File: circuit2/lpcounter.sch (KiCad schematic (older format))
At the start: 28 parts, among them IC1 ATTINY85V-P, M1 SYN115, P1 CONN_01X08, P10 BAT-, P2 CONN_02X01, P3 Hole_3.5mm, P4 Hole_3.5mm, P5 Hole_3.5mm, P6 Hole_3.5mm, P7 BAT+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

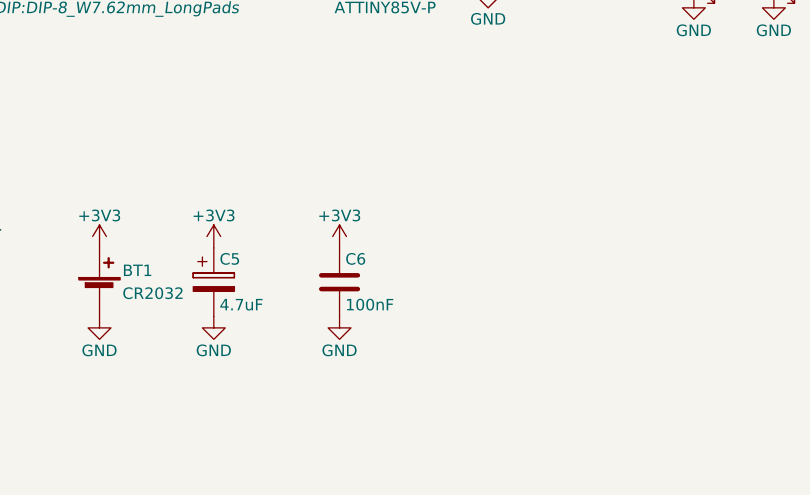
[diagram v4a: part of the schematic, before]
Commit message: small PCB optimizations, moving screw connector away from CR2032 battery add top zone layer and capacitor on top
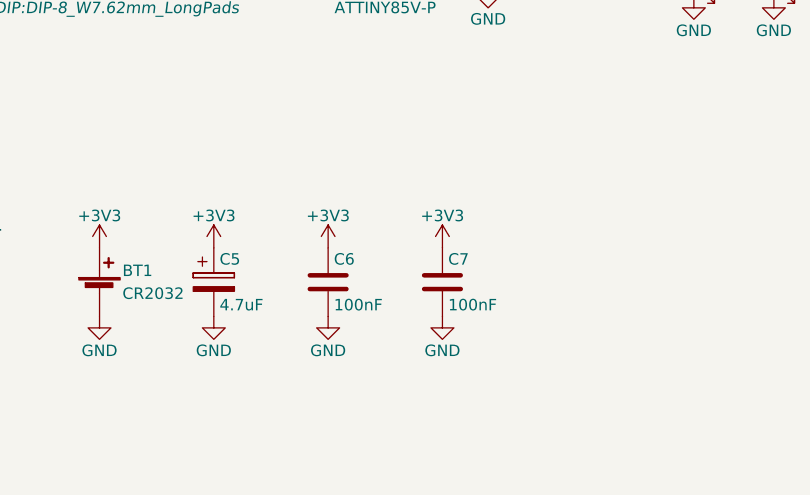
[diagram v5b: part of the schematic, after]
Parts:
- added C7: 100nF, Capacitors_SMD:C_1206_HandSoldering, symbol C
- D1: footprint Diodes_SMD:MELF_Handsoldering -> Diodes_SMD:MiniMELF_Handsoldering
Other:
- moved on the sheet: C6
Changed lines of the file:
@@
 IN0
 $Comp
-L GND #PWR01
+L GND #PWR30
 U 1 1 591028B9
 P 7900 3850
-F 0 "#PWR01" H 7900 3600 50  0001 C CNN
+F 0 "#PWR30" H 7900 3600 50  0001 C CNN
 F 1 "GND" H 7900 3700 50  0000 C CNN
 F 2 "" H 7900 3850 50  0000 C CNN
@@
 RESETn
 $Comp
-L +3V3 #PWR02
+L +3V3 #PWR29
 U 1 1 59102AB8
 P 7900 3250
-F 0 "#PWR02" H 7900 3100 50  0001 C CNN
+F 0 "#PWR29" H 7900 3100 50  0001 C CNN
 F 1 "+3V3" H 7900 3390 50  0000 C CNN
 F 2 "" H 7900 3250 50  0000 C CNN
@@
 F 0 "D1" H 5550 4800 50  0000 C CNN
 F 1 "1N4148" H 5550 4600 50  0000 C CNN
-F 2 "Diodes_SMD:MELF_Handsoldering" H 5550 4700 50  0001 C CNN
+F 2 "Diodes_SMD:MiniMELF_Handsoldering" H 5550 4700 50  0001 C CNN
 F 3 "" H 5550 4700 50  0000 C CNN
 	1    5550 4700
@@
 $EndComp
 $Comp
-L +3V3 #PWR03
+L +3V3 #PWR21
 U 1 1 59102B87
 P 6200 5000
-F 0 "#PWR03" H 6200 4850 50  0001 C CNN
+F 0 "#PWR21" H 6200 4850 50  0001 C CNN
 F 1 "+3V3" H 6200 5140 50  0000 C CNN
 F 2 "" H 6200 5000 50  0000 C CNN
@@
 $EndComp
 $Comp
-L GND #PWR04
+L GND #PWR22
 U 1 1 59102F4B
 P 6200 5300
-F 0 "#PWR04" H 6200 5050 50  0001 C CNN
+F 0 "#PWR22" H 6200 5050 50  0001 C CNN
 F 1 "GND" H 6200 5150 50  0000 C CNN
 F 2 "" H 6200 5300 50  0000 C CNN
@@
 ANT
 $Comp
-L GND #PWR05
+L GND #PWR33
 U 1 1 591034EC
 P 9750 3450
-F 0 "#PWR05" H 9750 3200 50  0001 C CNN
+F 0 "#PWR33" H 9750 3200 50  0001 C CNN
 F 1 "GND" H 9750 3300 50  0000 C CNN
 F 2 "" H 9750 3450 50  0000 C CNN
@@
 $EndComp
 $Comp
-L +3V3 #PWR06
+L +3V3 #PWR34
 U 1 1 59103508
 P 9750 3650
-F 0 "#PWR06" H 9750 3500 50  0001 C CNN
+F 0 "#PWR34" H 9750 3500 50  0001 C CNN
 F 1 "+3V3" H 9750 3790 50  0000 C CNN
 F 2 "" H 9750 3650 50  0000 C CNN
@@
 	1550 3850 2000 3850
 $Comp
-L GND #PWR07
+L GND #PWR2
 U 1 1 59103D18
 P 1550 3350
-F 0 "#PWR07" H 1550 3100 50  0001 C CNN
+F 0 "#PWR2" H 1550 3100 50  0001 C CNN
 F 1 "GND" H 1550 3200 50  0000 C CNN
 F 2 "" H 1550 3350 50  0000 C CNN
@@
 $EndComp
 $Comp
-L GND #PWR08
+L GND #PWR3
 U 1 1 59103D4F
 P 1550 3550
-F 0 "#PWR08" H 1550 3300 50  0001 C CNN
+F 0 "#PWR3" H 1550 3300 50  0001 C CNN
 F 1 "GND" H 1550 3400 50  0000 C CNN
 F 2 "" H 1550 3550 50  0000 C CNN
@@
 $EndComp
 $Comp
-L GND #PWR09
+L GND #PWR4
 U 1 1 59103D6D
 P 1550 3750
-F 0 "#PWR09" H 1550 3500 50  0001 C CNN
+F 0 "#PWR4" H 1550 3500 50  0001 C CNN
 F 1 "GND" H 1550 3600 50  0000 C CNN
 F 2 "" H 1550 3750 50  0000 C CNN
@@
 $EndComp
 $Comp
-L GND #PWR010
+L GND #PWR5
 U 1 1 59103DA4
 P 1550 3950
-F 0 "#PWR010" H 1550 3700 50  0001 C CNN
+F 0 "#PWR5" H 1550 3700 50  0001 C CNN
 F 1 "GND" H 1550 3800 50  0000 C CNN
 F 2 "" H 1550 3950 50  0000 C CNN
@@
 IN0
 $Comp
-L GND #PWR011
+L GND #PWR8
 U 1 1 5910458F
 P 2550 3900
-F 0 "#PWR011" H 2550 3650 50  0001 C CNN
+F 0 "#PWR8" H 2550 3650 50  0001 C CNN
 F 1 "GND" H 2550 3750 50  0000 C CNN
 F 2 "" H 2550 3900 50  0000 C CNN
@@
 $EndComp
 $Comp
-L +3V3 #PWR012
+L +3V3 #PWR7
 U 1 1 591045FE
 P 2550 3200
-F 0 "#PWR012" H 2550 3050 50  0001 C CNN
+F 0 "#PWR7" H 2550 3050 50  0001 C CNN
 F 1 "+3V3" H 2550 3340 50  0000 C CNN
 F 2 "" H 2550 3200 50  0000 C CNN
@@
 $EndComp
 $Comp
-L +3V3 #PWR013
+L +3V3 #PWR23
 U 1 1 5910481E
 P 6700 5000
-F 0 "#PWR013" H 6700 4850 50  0001 C CNN
+F 0 "#PWR23" H 6700 4850 50  0001 C CNN
 F 1 "+3V3" H 6700 5140 50  0000 C CNN
 F 2 "" H 6700 5000 50  0000 C CNN
@@
 $EndComp
 $Comp
-L GND #PWR014
+L GND #PWR24
 U 1 1 59104863
 P 6700 5300
-F 0 "#PWR014" H 6700 5050 50  0001 C CNN
+F 0 "#PWR24" H 6700 5050 50  0001 C CNN
 F 1 "GND" H 6700 5150 50  0000 C CNN
 F 2 "" H 6700 5300 50  0000 C CNN
@@
 IN1
 $Comp
-L GND #PWR015
+L GND #PWR11
 U 1 1 59104EB6
 P 3150 3900
-F 0 "#PWR015" H 3150 3650 50  0001 C CNN
+F 0 "#PWR11" H 3150 3650 50  0001 C CNN
 F 1 "GND" H 3150 3750 50  0000 C CNN
 F 2 "" H 3150 3900 50  0000 C CNN
@@
 $EndComp
 $Comp
-L +3V3 #PWR016
+L +3V3 #PWR10
 U 1 1 59104EBC
 P 3150 3200
-F 0 "#PWR016" H 3150 3050 50  0001 C CNN
+F 0 "#PWR10" H 3150 3050 50  0001 C CNN
 F 1 "+3V3" H 3150 3340 50  0000 C CNN
 F 2 "" H 3150 3200 50  0000 C CNN
@@
 IN2
 $Comp
-L GND #PWR017
+L GND #PWR13
 U 1 1 5910502C
 P 3750 3900
-F 0 "#PWR017" H 3750 3650 50  0001 C CNN
+F 0 "#PWR13" H 3750 3650 50  0001 C CNN
 F 1 "GND" H 3750 3750 50  0000 C CNN
 F 2 "" H 3750 3900 50  0000 C CNN
@@
 $EndComp
 $Comp
-L +3V3 #PWR018
+L +3V3 #PWR12
 U 1 1 59105032
 P 3750 3200
-F 0 "#PWR018" H 3750 3050 50  0001 C CNN
+F 0 "#PWR12" H 3750 3050 50  0001 C CNN
 F 1 "+3V3" H 3750 3340 50  0000 C CNN
 F 2 "" H 3750 3200 50  0000 C CNN
@@
 IN3
 $Comp
-L GND #PWR019
+L GND #PWR15
 U 1 1 59105048
 P 4350 3900
-F 0 "#PWR019" H 4350 3650 50  0001 C CNN
+F 0 "#PWR15" H 4350 3650 50  0001 C CNN
 F 1 "GND" H 4350 3750 50  0000 C CNN
 F 2 "" H 4350 3900 50  0000 C CNN
@@
 $EndComp
 $Comp
-L +3V3 #PWR020
+L +3V3 #PWR14
 U 1 1 5910504E
 P 4350 3200
-F 0 "#PWR020" H 4350 3050 50  0001 C CNN
+F 0 "#PWR14" H 4350 3050 50  0001 C CNN
 F 1 "+3V3" H 4350 3340 50  0000 C CNN
 F 2 "" H 4350 3200 50  0000 C CNN
@@
 	8250 3550 7950 3550
 $Comp
-L GND #PWR021
+L GND #PWR31
 U 1 1 59106156
 P 8800 3900
-F 0 "#PWR021" H 8800 3650 50  0001 C CNN
+F 0 "#PWR31" H 8800 3650 50  0001 C CNN
 F 1 "GND" H 8800 3750 50  0000 C CNN
 F 2 "" H 8800 3900 50  0000 C CNN
@@
 $EndComp
 $Comp
-L +3V3 #PWR022
+L +3V3 #PWR25
 U 1 1 5910891F
-P 7250 5000
-F 0 "#PWR022" H 7250 4850 50  0001 C CNN
-F 1 "+3V3" H 7250 5140 50  0000 C CNN
-F 2 "" H 7250 5000 50  0000 C CNN
-F 3 "" H 7250 5000 50  0000 C CNN
-	1    7250 5000
-	1    0    0    -1
-$EndComp
-$Comp
-L GND #PWR023
+P 7200 5000
+F 0 "#PWR25" H 7200 4850 50  0001 C CNN
+F 1 "+3V3" H 7200 5140 50  0000 C CNN
+F 2 "" H 7200 5000 50  0000 C CNN
+F 3 "" H 7200 5000 50  0000 C CNN
+	1    7200 5000
+	1    0    0    -1
+$EndComp
+$Comp
+L GND #PWR26
 U 1 1 59108925
-P 7250 5300
-F 0 "#PWR023" H 7250 5050 50  0001 C CNN
-F 1 "GND" H 7250 5150 50  0000 C CNN
-F 2 "" H 7250 5300 50  0000 C CNN
-F 3 "" H 7250 5300 50  0000 C CNN
-	1    7250 5300
+P 7200 5300
+F 0 "#PWR26" H 7200 5050 50  0001 C CNN
+F 1 "GND" H 7200 5150 50  0000 C CNN
+F 2 "" H 7200 5300 50  0000 C CNN
+F 3 "" H 7200 5300 50  0000 C CNN
+	1    7200 5300
 	1    0    0    -1
 $EndComp
@@
 L C C6
 U 1 1 59108977
-P 7250 5150
-F 0 "C6" H 7275 5250 50  0000 L CNN
-F 1 "100nF" H 7275 5050 50  0000 L CNN
-F 2 "Capacitors_SMD:C_1206_HandSoldering" H 7288 5000 50  0001 C CNN
-F 3 "" H 7250 5150 50  0000 C CNN
-	1    7250 5150
+P 7200 5150
+F 0 "C6" H 7225 5250 50  0000 L CNN
+F 1 "100nF" H 7225 5050 50  0000 L CNN
+F 2 "Capacitors_SMD:C_1206_HandSoldering" H 7238 5000 50  0001 C CNN
+F 3 "" H 7200 5150 50  0000 C CNN
+	1    7200 5150
 	1    0    0    -1
 $EndComp
@@
 $EndComp
 $Comp
-L +3V3 #PWR024
+L +3V3 #PWR16
 U 1 1 591067BD
 P 4350 4500
-F 0 "#PWR024" H 4350 4350 50  0001 C CNN
+F 0 "#PWR16" H 4350 4350 50  0001 C CNN
 F 1 "+3V3" H 4350 4640 50  0000 C CNN
 F 2 "" H 4350 4500 50  0000 C CNN
@@
 Connection ~ 4350 4950
 $Comp
-L GND #PWR025
+L GND #PWR17
 U 1 1 59106977
 P 4350 5500
-F 0 "#PWR025" H 4350 5250 50  0001 C CNN
+F 0 "#PWR17" H 4350 5250 50  0001 C CNN
 F 1 "GND" H 4350 5350 50  0000 C CNN
 F 2 "" H 4350 5500 50  0000 C CNN
@@
 $EndComp
 $Comp
-L GND #PWR026
+L GND #PWR6
 U 1 1 59119C8B
 P 2250 4800
-F 0 "#PWR026" H 2250 4550 50  0001 C CNN
+F 0 "#PWR6" H 2250 4550 50  0001 C CNN
 F 1 "GND" H 2250 4650 50  0000 C CNN
 F 2 "" H 2250 4800 50  0000 C CNN
@@
 $EndComp
 $Comp
-L GND #PWR027
+L GND #PWR9
 U 1 1 59119D27
 P 2800 4800
-F 0 "#PWR027" H 2800 4550 50  0001 C CNN
+F 0 "#PWR9" H 2800 4550 50  0001 C CNN
 F 1 "GND" H 2800 4650 50  0000 C CNN
 F 2 "" H 2800 4800 50  0000 C CNN
@@
 $EndComp
 $Comp
-L GND #PWR028
+L GND #PWR1
 U 1 1 59119EC9
 P 1150 4800
-F 0 "#PWR028" H 1150 4550 50  0001 C CNN
+F 0 "#PWR1" H 1150 4550 50  0001 C CNN
 F 1 "GND" H 1150 4650 50  0000 C CNN
 F 2 "" H 1150 4800 50  0000 C CNN
@@
 $EndComp
 $Comp
-L +3V3 #PWR029
+L +3V3 #PWR19
 U 1 1 5911EF06
 P 5550 4550
-F 0 "#PWR029" H 5550 4400 50  0001 C CNN
+F 0 "#PWR19" H 5550 4400 50  0001 C CNN
 F 1 "+3V3" H 5550 4690 50  0000 C CNN
 F 2 "" H 5550 4550 50  0000 C CNN
@@
 $EndComp
 $Comp
-L GND #PWR030
+L GND #PWR20
 U 1 1 591217AB
 P 5550 5800
-F 0 "#PWR030" H 5550 5550 50  0001 C CNN
+F 0 "#PWR20" H 5550 5550 50  0001 C CNN
 F 1 "GND" H 5550 5650 50  0000 C CNN
 F 2 "" H 5550 5800 50  0000 C CNN
@@
 Connection ~ 8800 3550
 $Comp
-L GND #PWR031
+L GND #PWR32
 U 1 1 5912DAF3
 P 9150 3900
-F 0 "#PWR031" H 9150 3650 50  0001 C CNN
+F 0 "#PWR32" H 9150 3650 50  0001 C CNN
 F 1 "GND" H 9150 3750 50  0000 C CNN
 F 2 "" H 9150 3900 50  0000 C CNN
@@
 $EndComp
 $Comp
-L GND #PWR032
+L GND #PWR18
 U 1 1 59172348
 P 5250 5800
-F 0 "#PWR032" H 5250 5550 50  0001 C CNN
+F 0 "#PWR18" H 5250 5550 50  0001 C CNN
 F 1 "GND" H 5250 5650 50  0000 C CNN
 F 2 "" H 5250 5800 50  0000 C CNN
@@
 	5250 5000 5550 5000
 Connection ~ 5550 5000
+$Comp
+L +3V3 #PWR27
+U 1 1 591AB77B
+P 7700 5000
+F 0 "#PWR27" H 7700 4850 50  0001 C CNN
+F 1 "+3V3" H 7700 5140 50  0000 C CNN
+F 2 "" H 7700 5000 50  0000 C CNN
+F 3 "" H 7700 5000 50  0000 C CNN
+	1    7700 5000
+	1    0    0    -1
+$EndComp
+$Comp
+L GND #PWR28
+U 1 1 591AB781
+P 7700 5300
+F 0 "#PWR28" H 7700 5050 50  0001 C CNN
+F 1 "GND" H 7700 5150 50  0000 C CNN
+F 2 "" H 7700 5300 50  0000 C CNN
+F 3 "" H 7700 5300 50  0000 C CNN
+	1    7700 5300
+	1    0    0    -1
+$EndComp
+$Comp
+L C C7
+U 1 1 591AB787
+P 7700 5150
+F 0 "C7" H 7725 5250 50  0000 L CNN
+F 1 "100nF" H 7725 5050 50  0000 L CNN
+F 2 "Capacitors_SMD:C_1206_HandSoldering" H 7738 5000 50  0001 C CNN
+F 3 "" H 7700 5150 50  0000 C CNN
+	1    7700 5150
+	1    0    0    -1
+$EndComp
 $EndSCHEMATC
